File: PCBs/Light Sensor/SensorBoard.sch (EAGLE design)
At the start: 35 parts, among them J1 AVR_SPI_PRG_6PTH, U2 MIC5219 3.3V

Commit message: Incremental updates
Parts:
- removed R2: 10, SparkFun-Passives:RESISTORAXIAL-0.3
- added R5: 1k, rcl:R-US_R1210
- R4: value (none) -> 1k
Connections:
- removed net N$1: JP3.VBUS, JP4.1, R1.1
- removed net N$2: R2.1, TINY.VCC
- new net VCC: JP3.VBUS, JP4.1, R1.1, TINY.VCC, XBEE.VCC
- net /XBEE_DEBUG: now also R5.1, XBEE.DTR; no longer R4.2
- net 3.3V: now also R4.2
- net 5V: no longer R2.2
- net GND: now also XBEE.GND
- net RADIO_OFF: now also U$5.A1
- net RST: now also R5.2; no longer R4.1
- net TINY_RX: now also U$8.A1
- net TINY_TX: now also U$5.A2
- net XBEE_DTR: now also R4.1; no longer XBEE.DTR
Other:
- note removed: "NOTE: DTR normally high. Active low to indicate computer connection."
- moved on the sheet: R1, R4, XBEE

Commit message: Still routing and placing
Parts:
- U$6: value XBEE-1B1 -> XBEE-2B1; device MyLibrary:XBEE-1B1 -> SparkFun-RF:XBEE-2B1
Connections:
- net 3.3V: now also U$7.(PCINT0/AREF/ADC0)PA0; no longer U$7.(PCINT1/AIN0/ADC1)PA1
- net AUX_ANALOG: now also U$7.(PCINT1/AIN0/ADC1)PA1; no longer U$7.(PCINT0/AREF/ADC0)PA0
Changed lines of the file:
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@@
 <part name="SUPPLY2" library="SparkFun-Aesthetics" deviceset="3.3V" device=""/>
 <part name="SUPPLY3" library="SparkFun-Aesthetics" deviceset="3.3V" device=""/>
-<part name="U$6" library="MyLibrary" deviceset="XBEE-1" device="B1"/>
+<part name="U$6" library="SparkFun-RF" deviceset="XBEE-2" device="B1"/>
 <part name="J1" library="SparkFun-Connectors" deviceset="AVR_SPI_PRG_6" device="PTH"/>
 <part name="SUPPLY4" library="SparkFun-Aesthetics" deviceset="5V" device=""/>
@@
 </segment>
 <segment>
-<pinref part="U$7" gate="G$1" pin="(PCINT1/AIN0/ADC1)PA1"/>
-<wire x1="137.16" y1="111.76" x2="149.86" y2="111.76" width="0.1524" layer="91"/>
-<label x="139.7" y="111.76" size="1.778" layer="95"/>
-</segment>
-<segment>
 <pinref part="U2" gate="G$1" pin="OUT"/>
 <pinref part="SUPPLY2" gate="G$1" pin="3.3V"/>
@@
 <wire x1="182.88" y1="109.22" x2="182.88" y2="114.3" width="0.1524" layer="91"/>
 <junction x="182.88" y="114.3"/>
+</segment>
+<segment>
+<pinref part="U$7" gate="G$1" pin="(PCINT0/AREF/ADC0)PA0"/>
+<wire x1="137.16" y1="109.22" x2="149.86" y2="109.22" width="0.1524" layer="91"/>
+<label x="139.7" y="109.22" size="1.778" layer="95"/>
 </segment>
 </net>
@@
 </segment>
 </net>
-<net name="AUX_ANALOG" class="0">
-<segment>
-<pinref part="U$7" gate="G$1" pin="(PCINT0/AREF/ADC0)PA0"/>
-<wire x1="137.16" y1="109.22" x2="149.86" y2="109.22" width="0.1524" layer="91"/>
-<label x="139.7" y="109.22" size="1.778" layer="95"/>
-</segment>
-</net>
 <net name="N$3" class="0">
 <segment>
@@
 </segment>
 </net>
+<net name="AUX_ANALOG" class="1">
+<segment>
+<pinref part="U$7" gate="G$1" pin="(PCINT1/AIN0/ADC1)PA1"/>
+<wire x1="137.16" y1="111.76" x2="149.86" y2="111.76" width="0.1524" layer="91"/>
+<label x="139.7" y="111.76" size="1.778" layer="95"/>
+</segment>
+</net>

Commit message: Almost finished with layout
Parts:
- added R2: 1k, rcl:R-US_R1210
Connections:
- net 3.3V_ENABLE: now also R2.1
- net 5V: now also R2.2
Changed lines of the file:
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@@
 <clearance class="0" value="0.1524"/>
 </class>
-<class number="1" name="power" width="0.3048" drill="0.3302">
+<class number="1" name="power" width="0.1524" drill="0.3302">
 <clearance class="1" value="0.1524"/>
 </class>
@@
 <part name="GND6" library="supply1" deviceset="GND" device=""/>
 <part name="SUPPLY8" library="supply2" deviceset="VCC" device=""/>
+<part name="SUPPLY11" library="SparkFun-Aesthetics" deviceset="5V" device=""/>
+<part name="SUPPLY17" library="supply2" deviceset="VCC" device=""/>
 <part name="SUPPLY7" library="supply2" deviceset="VCC" device=""/>
 <part name="SUPPLY9" library="supply2" deviceset="VCC" device=""/>
-<part name="SUPPLY11" library="SparkFun-Aesthetics" deviceset="5V" device=""/>
-<part name="SUPPLY17" library="supply2" deviceset="VCC" device=""/>
+<part name="R2" library="rcl" deviceset="R-US_" device="R1210" value="1k"/>
+<part name="SUPPLY18" library="SparkFun-Aesthetics" deviceset="5V" device=""/>
 </parts>
 <sheets>
@@
 <instance part="GND6" gate="1" x="220.98" y="45.72"/>
 <instance part="SUPPLY8" gate="G$1" x="99.06" y="170.18"/>
-<instance part="SUPPLY7" gate="G$1" x="25.4" y="38.1"/>
-<instance part="SUPPLY9" gate="G$1" x="200.66" y="55.88" rot="R90"/>
 <instance part="SUPPLY11" gate="G$1" x="83.82" y="167.64"/>
 <instance part="SUPPLY17" gate="G$1" x="7.62" y="132.08"/>
+<instance part="SUPPLY7" gate="G$1" x="25.4" y="38.1"/>
+<instance part="SUPPLY9" gate="G$1" x="198.12" y="55.88" rot="R90"/>
+<instance part="R2" gate="G$1" x="63.5" y="129.54" rot="R90"/>
+<instance part="SUPPLY18" gate="G$1" x="63.5" y="137.16"/>
 </instances>
 <busses>
@@
 <pinref part="R1" gate="G$1" pin="2"/>
 <wire x1="83.82" y1="162.56" x2="86.36" y2="162.56" width="0.1524" layer="91"/>
+</segment>
+<segment>
+<pinref part="R2" gate="G$1" pin="2"/>
+<pinref part="SUPPLY18" gate="G$1" pin="5V"/>
+<wire x1="63.5" y1="134.62" x2="63.5" y2="137.16" width="0.1524" layer="91"/>
 </segment>
 </net>
@@
 <pinref part="U2" gate="G$1" pin="EN"/>
 <wire x1="50.8" y1="162.56" x2="48.26" y2="162.56" width="0.1524" layer="91"/>
-<wire x1="48.26" y1="162.56" x2="48.26" y2="139.7" width="0.1524" layer="91"/>
-<wire x1="48.26" y1="139.7" x2="63.5" y2="139.7" width="0.1524" layer="91"/>
-<label x="50.8" y="139.7" size="1.778" layer="95"/>
+<wire x1="48.26" y1="162.56" x2="48.26" y2="121.92" width="0.1524" layer="91"/>
+<wire x1="48.26" y1="121.92" x2="63.5" y2="121.92" width="0.1524" layer="91"/>
+<label x="48.26" y="119.38" size="1.778" layer="95"/>
+<pinref part="R2" gate="G$1" pin="1"/>
+<wire x1="63.5" y1="121.92" x2="63.5" y2="124.46" width="0.1524" layer="91"/>
 </segment>
 </net>
@@
 <net name="VCC" class="0">
 <segment>
-<pinref part="TINY" gate="G$1" pin="VCC"/>
-<wire x1="27.94" y1="25.4" x2="25.4" y2="25.4" width="0.1524" layer="91"/>
-<wire x1="25.4" y1="25.4" x2="25.4" y2="35.56" width="0.1524" layer="91"/>
-<pinref part="SUPPLY7" gate="G$1" pin="VCC"/>
-</segment>
-<segment>
-<pinref part="XBEE" gate="G$1" pin="VCC"/>
-<wire x1="203.2" y1="55.88" x2="223.52" y2="55.88" width="0.1524" layer="91"/>
-<pinref part="SUPPLY9" gate="G$1" pin="VCC"/>
-</segment>
-<segment>
 <pinref part="R1" gate="G$1" pin="1"/>
 <pinref part="SUPPLY8" gate="G$1" pin="VCC"/>
@@
 <junction x="7.62" y="121.92"/>
 </segment>
-</net>
+<segment>
+<pinref part="TINY" gate="G$1" pin="VCC"/>
+<pinref part="SUPPLY7" gate="G$1" pin="VCC"/>
+<wire x1="27.94" y1="25.4" x2="25.4" y2="25.4" width="0.1524" layer="91"/>
+<wire x1="25.4" y1="25.4" x2="25.4" y2="35.56" width="0.1524" layer="91"/>
+</segment>
+<segment>
+<pinref part="SUPPLY9" gate="G$1" pin="VCC"/>
+<pinref part="XBEE" gate="G$1" pin="VCC"/>
+<wire x1="200.66" y1="55.88" x2="223.52" y2="55.88" width="0.1524" layer="91"/>
+</segment>
+</net>

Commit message: Rev. B layout complete, design review soon
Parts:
- removed STANDOFF1, STANDOFF2, STANDOFF3: STAND-OFF, SparkFun-Electromechanical:STAND-OFF
- removed U$7: ATTINY84, SparkFun-DigitalIC:ATTINY84
- removed U$8: SN74LVC2T45, MyLibrary:SN74LVC2T45
- added R6: 1k, rcl:R-US_R1210
- added U1: APDS-9008, MyLibrary:APDS-9008
- added U3: OPT101TH, MyLibrary:OPT101TH
- added U4: ATTINY84HANDSOLDER, MyLibrary:ATTINY84HANDSOLDER
- C1: value 0.1uf -> 470pF
- C2: value 8.2pf -> 0.1uf
- C3: value 1.0uf -> 0.1uf
- C4: value 10uf -> 8.2pf
- C5: value 0.1uf -> 1.0uf
- C6: value 470pF -> 10uf
- R1: value 10 -> 1k; device SparkFun-Passives:RESISTORAXIAL-0.3 -> rcl:R-US_R1210
- R2: value 1k -> 10; device rcl:R-US_R1210 -> SparkFun-Passives:RESISTORAXIAL-0.3
- U$2: value APDS-9008 -> PROTOAREA-10X10; device MyLibrary:APDS-9008 -> MyLibrary:PROTOAREA-10X10
- U$3: value PROTOAREA-10X10 -> SN74LVC1T45; device MyLibrary:PROTOAREA-10X10 -> MyLibrary:SN74LVC1T45
- U$4: value OPT101TH -> SN74LVC1T45; device MyLibrary:OPT101TH -> MyLibrary:SN74LVC1T45
- U$5: value SN74LVC2T45 -> SN74LVC1T45; device MyLibrary:SN74LVC2T45 -> MyLibrary:SN74LVC1T45
- U2: value MIC5219 3.3V -> MIC5219
- renumbered U$6 to U5
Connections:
- removed net RADIO_OFF: U$5.A1, U$7.(PCINT10/INT0/OC0A/CKOUT)PB2
- new net RADIO_ON: U$3.A, U4.(PCINT10/INT0/OC0A/CKOUT)PB2
- net /XBEE_DEBUG: now also R4.1, U$3.DIR, U$4.DIR; no longer R5.1, U$5.DIR
- net 3.3V: now also C6.1, C8.1, R5.2, U$3.VB, U$4.VB, U1.VCC, U3.1, U4.(PCINT0/AREF/ADC0)PA0; no longer C2.1, C3.1, R4.2, U$2.VCC, U$4.1, U$7.(PCINT0/AREF/ADC0)PA0, U$8.VB
- net 3.3V_ENABLE: now also R1.1, U4.(PCINT7/ICP/OC0B/ADC7)PA7; no longer R2.1, U$7.(PCINT7/ICP/OC0B/ADC7)PA7
- net 5V: now also C2.1, C3.1, U$3.VA, U$4.VA, U4.VCC; no longer C1.1, C8.1, U$7.VCC, U$8.VA
- net APDS_9008: now also R6.2, U1.OUT, U4.(PCINT3/T0/ADC3)PA3; no longer U$2.OUT, U$7.(PCINT2/AIN1/ADC2)PA2
- net AUX_ANALOG: now also U4.(PCINT1/AIN0/ADC1)PA1; no longer U$7.(PCINT1/AIN0/ADC1)PA1
- net GND: now also R6.1, U$3.GND, U$4.GND, U$5.DIR, U1.GND, U3.3, U3.8, U4.GND; no longer U$2.GND, U$4.3, U$4.8, U$7.GND, U$8.DIR, U$8.GND
- net MISO: now also U4.(PCINT5/OC1B/MISO/DO/ADC5)PA5; no longer U$7.(PCINT5/OC1B/MISO/DO/ADC5)PA5
- net MOSI: now also U4.(PCINT6/OC1A/SDA/MOSI/ADC6)PA6; no longer U$7.(PCINT6/OC1A/SDA/MOSI/ADC6)PA6
- net N$3: now also C1.1; no longer C6.1
- net OPT_101: now also U3.4, U3.5, U4.(PCINT2/AIN1/ADC2)PA2; no longer U$4.4, U$4.5, U$7.(PCINT3/T0/ADC3)PA3
- net RST: now also R4.2, U4.(PCINT11/~RESET/DW)PB3; no longer R5.2, U$7.(PCINT11/~RESET/DW)PB3
- net SCK: now also U4.(PCINT4/T1/SCL/USCK/ADC4)PA4; no longer U$7.(PCINT4/T1/SCL/USCK/ADC4)PA4
- net TINY_RX: now also U$5.A, U4.(PCINT8/XTAL1/CLKI)PB0; no longer U$7.(PCINT8/XTAL1/CLKI)PB0, U$8.A1
- net TINY_TX: now also U$4.A, U4.(PCINT9/XTAL2)PB1; no longer U$5.A2, U$7.(PCINT9/XTAL2)PB1
- net VCC: now also R2.1; no longer R1.1
- net XBEE_DTR: now also R5.1, U$3.B; no longer R4.1, U$5.B1
- net XBEE_RX: now also U$4.B; no longer U$5.B2
- net XBEE_TX: now also U$5.B; no longer U$8.B1
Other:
- moved on the sheet: C1, C2, C3, C4, C5, C6, C7, C8, R1, R2, R4, R5

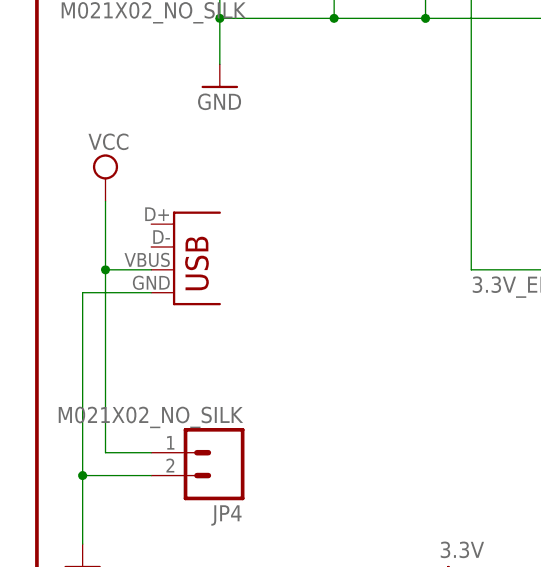
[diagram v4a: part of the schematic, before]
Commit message: Grounded USB shield
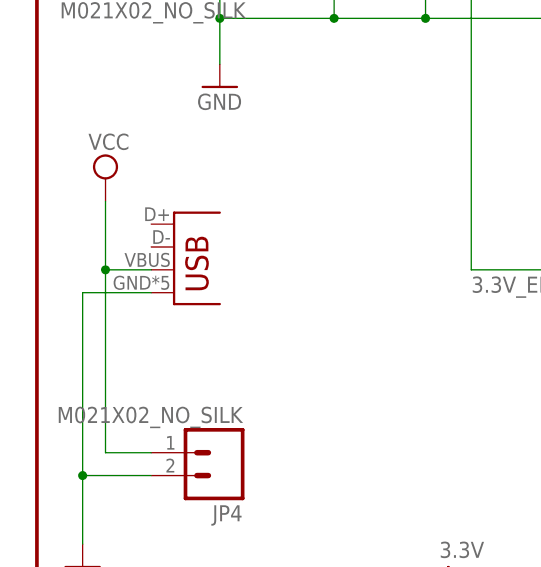
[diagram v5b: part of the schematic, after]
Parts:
- FRAME1: device SparkFun-Aesthetics:FRAME-LETTER -> MyLibrary:FRAME-LETTER
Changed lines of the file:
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@@
 <part name="JP1" library="SparkFun-Connectors" deviceset="M02" device="1X02_NO_SILK" value="M021X02_NO_SILK"/>
 <part name="JP2" library="SparkFun-Connectors" deviceset="M02" device="1X02_NO_SILK" value="M021X02_NO_SILK"/>
-<part name="JP3" library="SparkFun-Connectors" deviceset="USB" device="SMD"/>
 <part name="R2" library="SparkFun-Passives" deviceset="RESISTOR" device="AXIAL-0.3" value="10"/>
 <part name="GND10" library="supply1" deviceset="GND" device=""/>
-<part name="FRAME1" library="SparkFun-Aesthetics" deviceset="FRAME-LETTER" device=""/>
+<part name="FRAME1" library="MyLibrary" deviceset="FRAME-LETTER" device=""/>
 <part name="U$2" library="MyLibrary" deviceset="PROTOAREA-10X10" device=""/>
 <part name="JP7" library="SparkFun-Connectors" deviceset="M04" device="1X04_NO_SILK"/>
@@
 <part name="R6" library="rcl" deviceset="R-US_" device="R1210" value="1k"/>
 <part name="GND13" library="supply1" deviceset="GND" device=""/>
+<part name="JP3" library="SparkFun-Connectors" deviceset="USB" device="SMD"/>
 </parts>
 <sheets>
@@
 <instance part="JP1" gate="G$1" x="5.08" y="167.64"/>
 <instance part="JP2" gate="G$1" x="5.08" y="154.94"/>
-<instance part="JP3" gate="G$1" x="15.24" y="119.38"/>
 <instance part="R2" gate="G$1" x="91.44" y="162.56" rot="R180"/>
 <instance part="GND10" gate="1" x="5.08" y="88.9"/>
-<instance part="FRAME1" gate="G$1" x="0" y="0"/>
+<instance part="FRAME1" gate="G$1" x="0" y="0" smashed="yes"/>
 <instance part="FRAME1" gate="G$2" x="147.32" y="0"/>
 <instance part="U$2" gate="G$1" x="55.88" y="7.62"/>
@@
 <instance part="R6" gate="G$1" x="66.04" y="60.96" rot="R90"/>
 <instance part="GND13" gate="1" x="66.04" y="48.26"/>
+<instance part="JP3" gate="G$1" x="15.24" y="119.38"/>
 </instances>
 <busses>
@@
 </segment>
 <segment>
-<pinref part="JP3" gate="G$1" pin="GND"/>
 <pinref part="GND10" gate="1" pin="GND"/>
 <wire x1="12.7" y1="119.38" x2="5.08" y2="119.38" width="0.1524" layer="91"/>
@@
 <wire x1="12.7" y1="99.06" x2="5.08" y2="99.06" width="0.1524" layer="91"/>
 <junction x="5.08" y="99.06"/>
+<pinref part="JP3" gate="G$1" pin="GND"/>
 </segment>
 <segment>
@@
 </segment>
 <segment>
-<pinref part="JP3" gate="G$1" pin="VBUS"/>
 <wire x1="12.7" y1="121.92" x2="7.62" y2="121.92" width="0.1524" layer="91"/>
 <wire x1="7.62" y1="121.92" x2="7.62" y2="101.6" width="0.1524" layer="91"/>
@@
 <wire x1="7.62" y1="121.92" x2="7.62" y2="129.54" width="0.1524" layer="91"/>
 <junction x="7.62" y="121.92"/>
-</segment>
-<segment>
+<pinref part="JP3" gate="G$1" pin="VBUS"/>
+</segment>
+<segment>

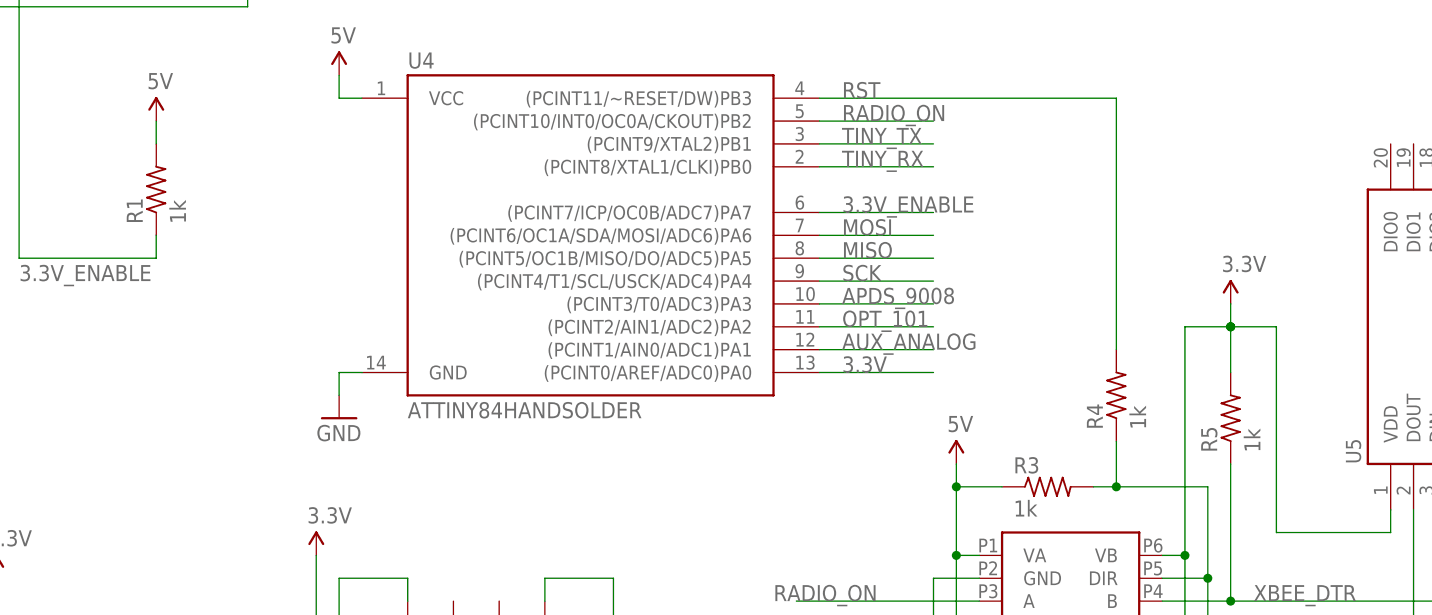
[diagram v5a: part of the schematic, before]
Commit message: Changed pullups to 100K to save power
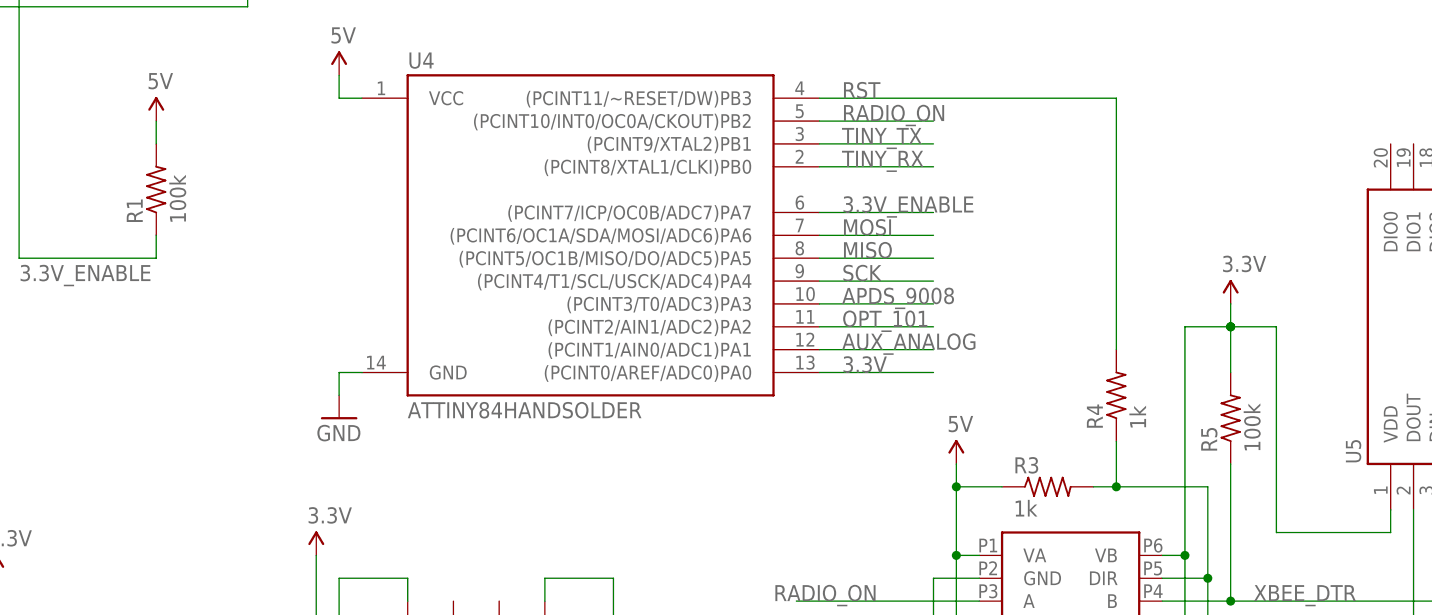
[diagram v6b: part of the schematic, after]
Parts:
- R1, R5: value 1k -> 100k
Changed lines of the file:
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@@
 <part name="R3" library="rcl" deviceset="R-US_" device="R1210" value="1k"/>
 <part name="SUPPLY16" library="SparkFun-Aesthetics" deviceset="3.3V" device=""/>
-<part name="R5" library="rcl" deviceset="R-US_" device="R1210" value="1k"/>
+<part name="R5" library="rcl" deviceset="R-US_" device="R1210" value="100k"/>
 <part name="R4" library="rcl" deviceset="R-US_" device="R1210" value="1k"/>
 <part name="GND6" library="supply1" deviceset="GND" device=""/>
@@
 <part name="SUPPLY7" library="supply2" deviceset="VCC" device=""/>
 <part name="SUPPLY9" library="supply2" deviceset="VCC" device=""/>
-<part name="R1" library="rcl" deviceset="R-US_" device="R1210" value="1k"/>
+<part name="R1" library="rcl" deviceset="R-US_" device="R1210" value="100k"/>
 <part name="SUPPLY18" library="SparkFun-Aesthetics" deviceset="5V" device=""/>
 <part name="U$3" library="MyLibrary" deviceset="SN74LVC1T45" device=""/>
